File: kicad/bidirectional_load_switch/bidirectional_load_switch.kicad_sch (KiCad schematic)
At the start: 30 parts, among them J102 Conn_01x02_Socket, J103 Conn_01x09_Socket, J104 Conn_01x02_Socket, J105 Conn_01x02_Socket, J106 Conn_01x02_Socket, J107 AVR-ISP-6

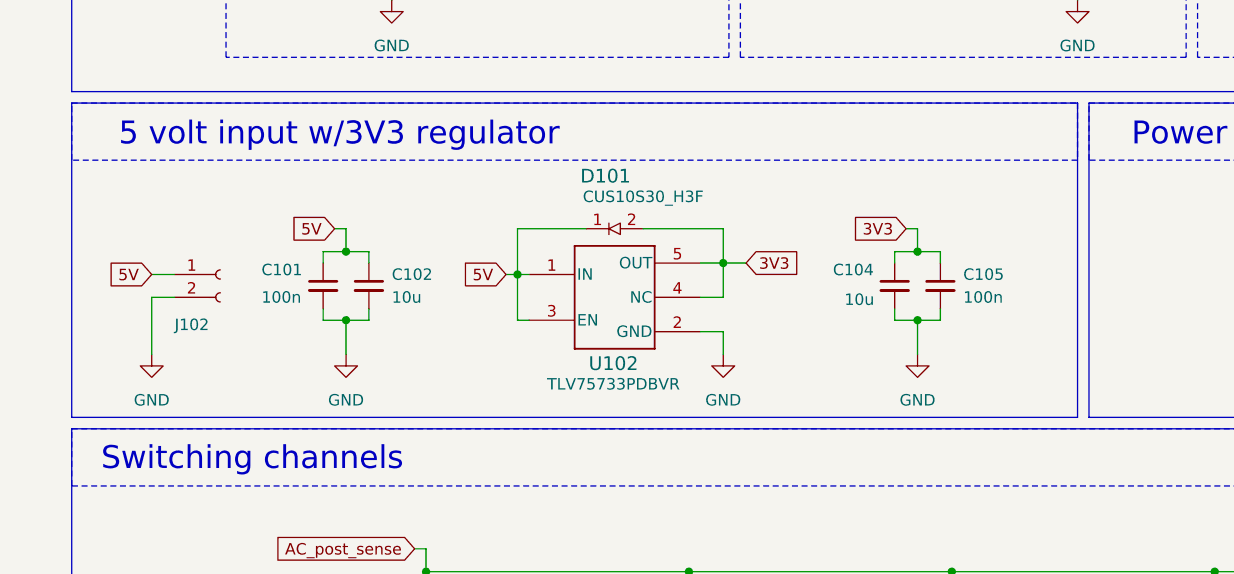
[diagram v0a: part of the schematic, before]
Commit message: implementing 5v and 3v3 supply ORing
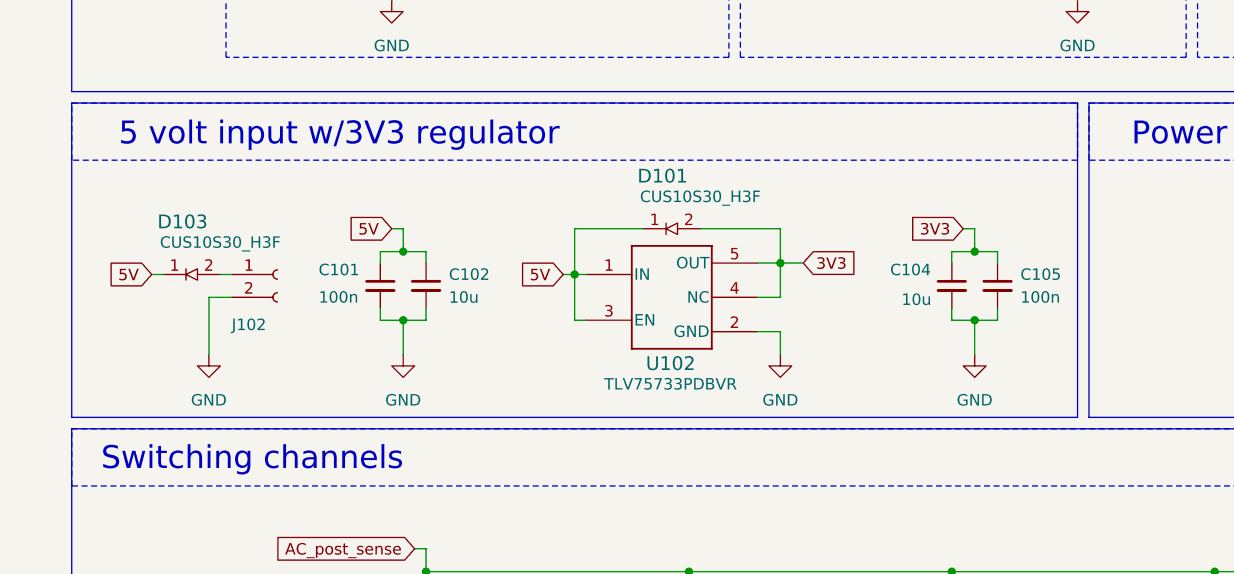
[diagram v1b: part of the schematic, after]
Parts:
- added D103: ~, diode_CUS10S30_H3F:USC_TOS, symbol diode_CUS10S30_H3F:CUS10S30_H3F
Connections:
- net 5V: now also D103.1; no longer J102.1 (Pin_1)
- new net: D103.2, J102.1 (Pin_1)
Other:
- moved on the sheet: C101, C102, C104, C105, D101, J102, U102

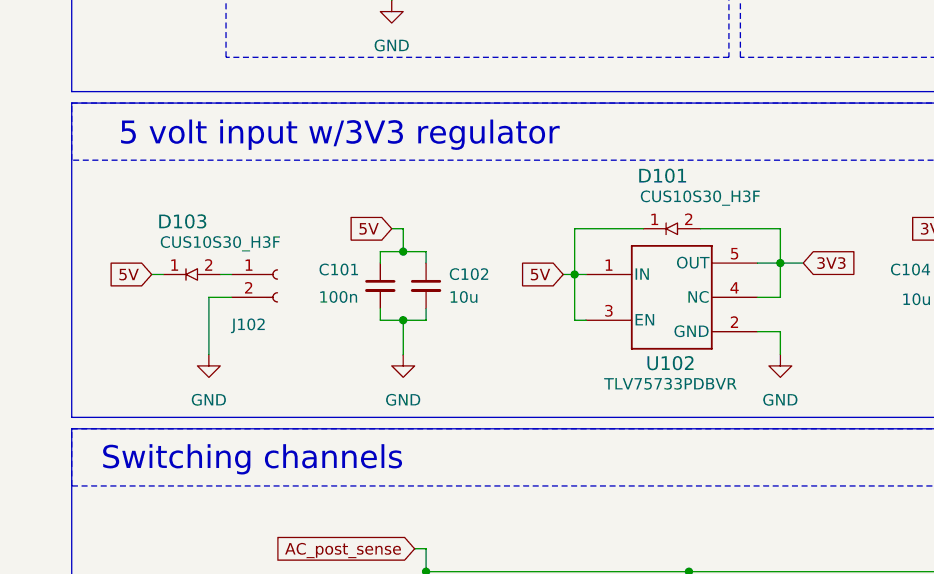
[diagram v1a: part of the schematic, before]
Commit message: added 5v and 3v3 supply ORing and revised silkscreen text
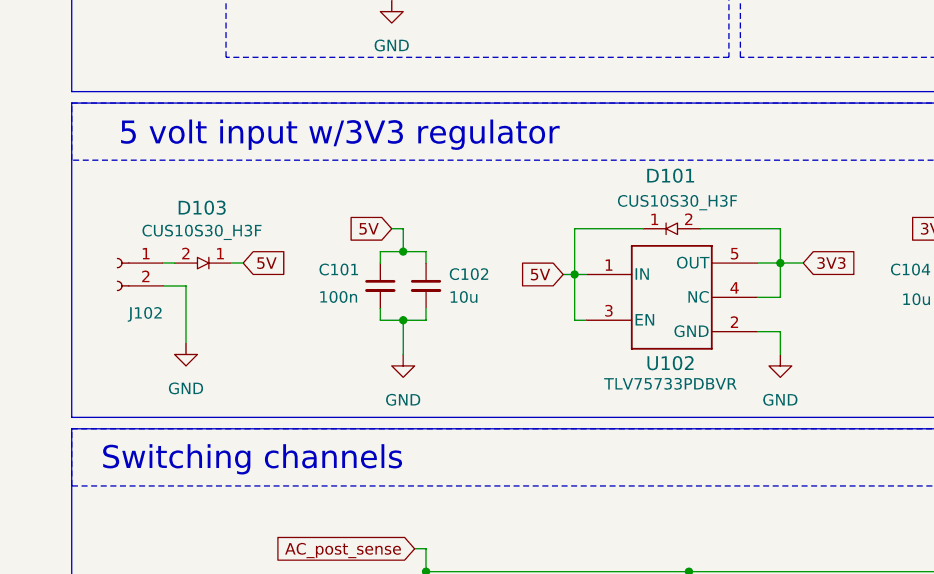
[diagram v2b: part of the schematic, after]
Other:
- moved on the sheet: D103, J102
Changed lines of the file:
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@@
 	(wire
 		(pts
-			(xy 25.4 87.63) (xy 26.67 87.63)
+			(xy 35.56 86.36) (xy 34.29 86.36)
 		)
 		(stroke
@@
 	(wire
 		(pts
-			(xy 31.75 90.17) (xy 34.29 90.17)
+			(xy 29.21 88.9) (xy 26.67 88.9)
 		)
 		(stroke
@@
 	(wire
 		(pts
-			(xy 33.02 87.63) (xy 34.29 87.63)
+			(xy 27.94 86.36) (xy 26.67 86.36)
 		)
 		(stroke
@@
 	(wire
 		(pts
-			(xy 31.75 96.52) (xy 31.75 90.17)
+			(xy 29.21 95.25) (xy 29.21 88.9)
 		)
 		(stroke
@@
 	(global_label "5V"
 		(shape input)
-		(at 25.4 87.63 180)
+		(at 35.56 86.36 0)
 		(fields_autoplaced yes)
 		(effects
@@
 				(size 1.27 1.27)
 			)
-			(justify right)
+			(justify left)
 		)
 		(property "Intersheetrefs" "${INTERSHEET_REFS}"
-			(at 20.1167 87.63 0)
+			(at 40.8433 86.36 0)
 			(effects
 				(font
 					(size 1.27 1.27)
 				)
-				(justify right)
+				(justify left)
 				(hide yes)
 			)
@@
 	(symbol
 		(lib_id "Connector:Conn_01x02_Socket")
-		(at 39.37 87.63 0)
+		(at 21.59 86.36 0)
+		(mirror y)
 		(unit 1)
 		(exclude_from_sim no)
@@
 		(dnp no)
 		(property "Reference" "J102"
-			(at 34.29 93.218 0)
+			(at 26.67 91.948 0)
 			(effects
 				(font
@@
 		)
 		(property "Value" "Conn_01x02_Socket"
-			(at 40.64 90.1699 0)
+			(at 20.32 88.8999 0)
 			(effects
 				(font
@@
 		)
 		(property "Footprint" "Connector_PinHeader_2.54mm:PinHeader_1x02_P2.54mm_Vertical"
-			(at 39.37 87.63 0)
+			(at 21.59 86.36 0)
 			(effects
 				(font
@@
 		)
 		(property "Datasheet" "~"
-			(at 39.37 87.63 0)
+			(at 21.59 86.36 0)
 			(effects
 				(font
@@
 		)
 		(property "Description" "Generic connector, single row, 01x02, script generated"
-			(at 39.37 87.63 0)
+			(at 21.59 86.36 0)
 			(effects
 				(font
@@
 	(symbol
 		(lib_id "power:GND")
-		(at 31.75 96.52 0)
+		(at 29.21 95.25 0)
+		(mirror y)
 		(unit 1)
 		(exclude_from_sim no)
@@
 		(fields_autoplaced yes)
 		(property "Reference" "#PWR0101"
-			(at 31.75 102.87 0)
+			(at 29.21 101.6 0)
 			(effects
 				(font
@@
 		)
 		(property "Value" "GND"
-			(at 31.75 101.6 0)
+			(at 29.21 100.33 0)
 			(effects
 				(font
@@
 		)
 		(property "Footprint" ""
-			(at 31.75 96.52 0)
+			(at 29.21 95.25 0)
 			(effects
 				(font
@@
 		)
 		(property "Datasheet" ""
-			(at 31.75 96.52 0)
+			(at 29.21 95.25 0)
 			(effects
 				(font
@@
 		)
 		(property "Description" "Power symbol creates a global label with name \"GND\" , ground"
-			(at 31.75 96.52 0)
+			(at 29.21 95.25 0)
 			(effects
 				(font
@@
 		(dnp no)
 		(property "Reference" "D101"
-			(at 82.169 76.708 0)
+			(at 83.058 76.708 0)
 			(effects
 				(font
@@
 		)
 		(property "MPN" "CUS10S30_H3F"
-			(at 86.36 78.994 0)
+			(at 83.82 79.502 0)
 			(effects
 				(font
@@
 	(symbol
 		(lib_id "diode_CUS10S30_H3F:CUS10S30_H3F")
-		(at 33.02 87.63 180)
+		(at 27.94 86.36 0)
+		(mirror x)
 		(unit 1)
 		(exclude_from_sim no)
@@
 		(dnp no)
 		(property "Reference" "D103"
-			(at 28.829 81.788 0)
+			(at 30.988 80.264 0)
 			(effects
 				(font
@@
 		)
 		(property "Value" "~"
-			(at 28.829 84.328 0)
+			(at 32.131 83.058 0)
 			(effects
 				(font
@@
 		)
 		(property "Footprint" "diode_CUS10S30_H3F:USC_TOS"
-			(at 41.021 93.218 0)
+			(at 19.939 91.948 0)
 			(effects
 				(font
@@
 		)
 		(property "Datasheet" "https://toshiba.semicon-storage.com/info/CUS10S30_datasheet_en_20140407.pdf?did=14077&prodName=CUS10S30"
-			(at 40.005 94.996 0)
+			(at 20.955 93.726 0)
 			(effects
 				(font
@@
 		)
 		(property "Description" ""
-			(at 32.385 87.63 0)
+			(at 28.575 86.36 0)
 			(effects
 				(font
@@
 		)
 		(property "MPN" "CUS10S30_H3F"
-			(at 33.02 84.074 0)
+			(at 30.988 82.804 0)
 			(effects
 				(font
